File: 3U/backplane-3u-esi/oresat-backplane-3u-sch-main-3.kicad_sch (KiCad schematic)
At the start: 30 parts

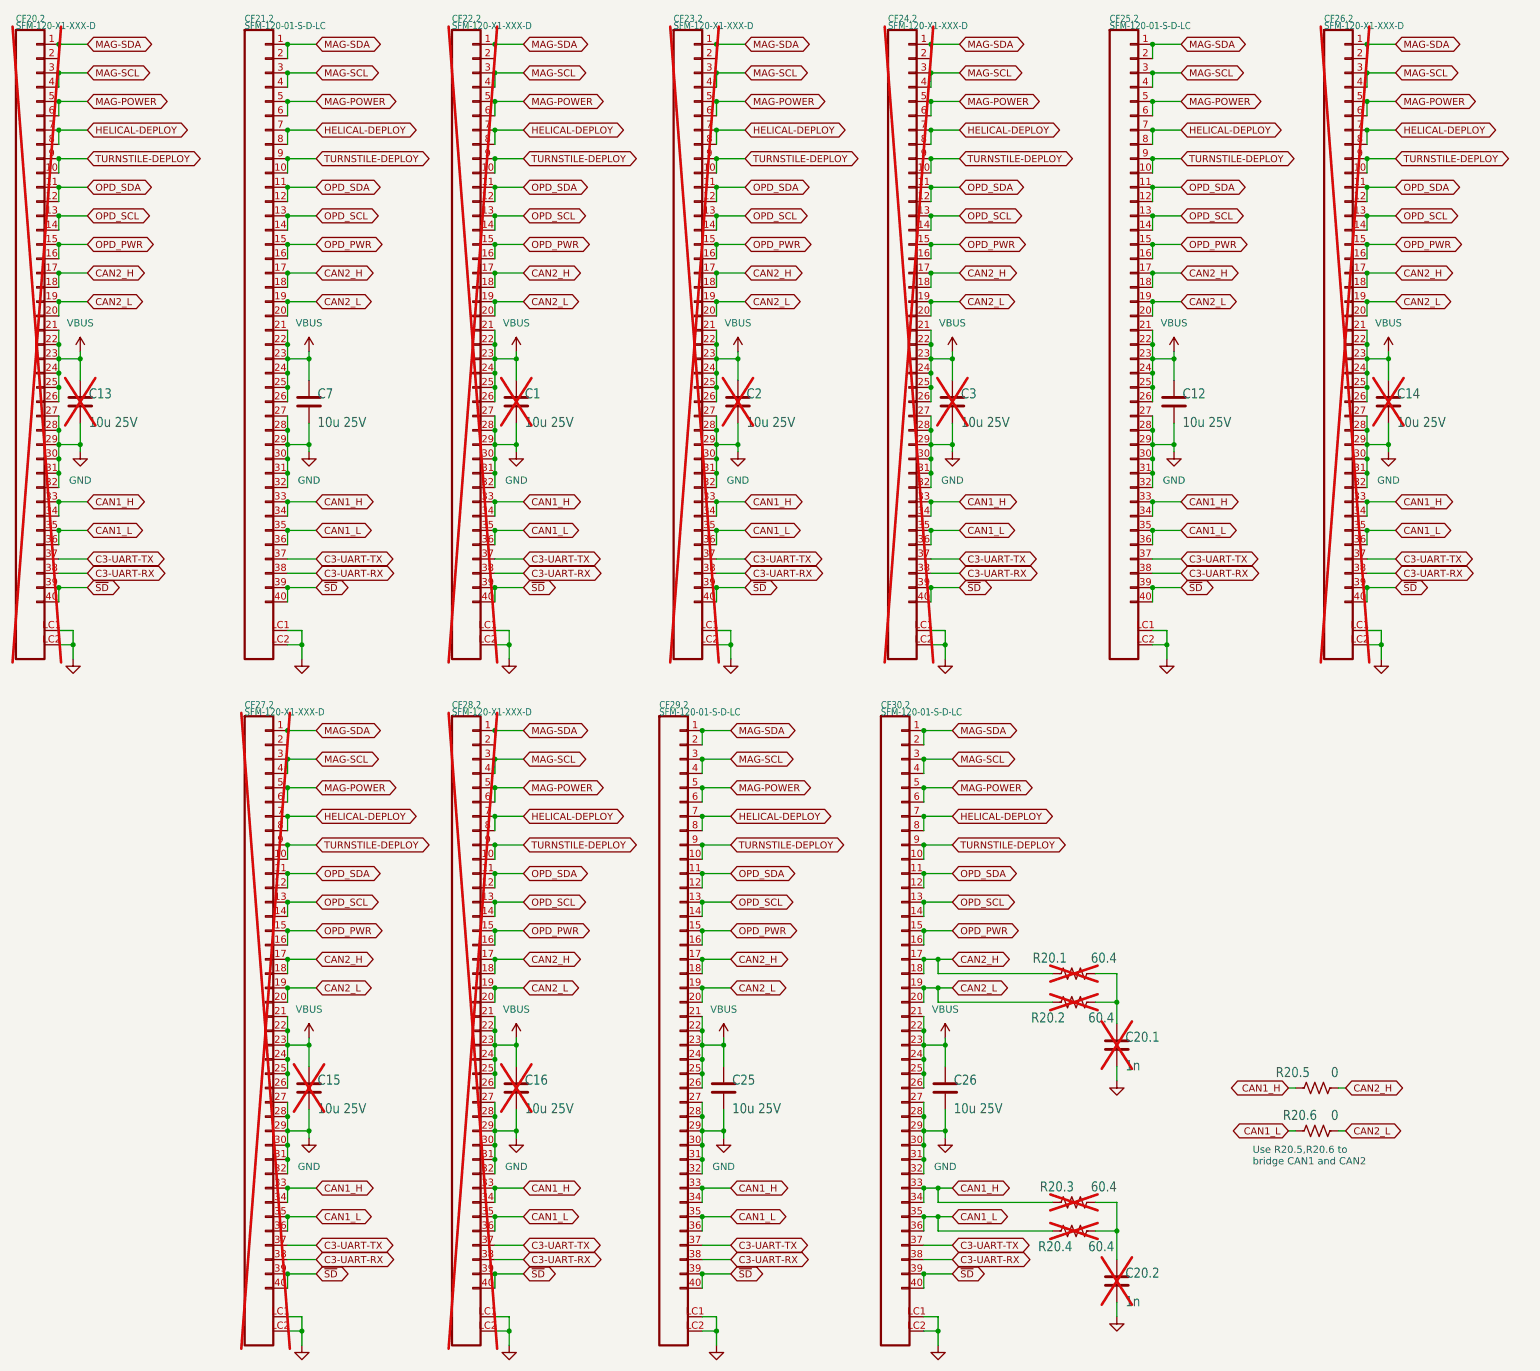
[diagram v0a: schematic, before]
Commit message: Changed schematic & pcb to add spare traces, no helical or turnstile
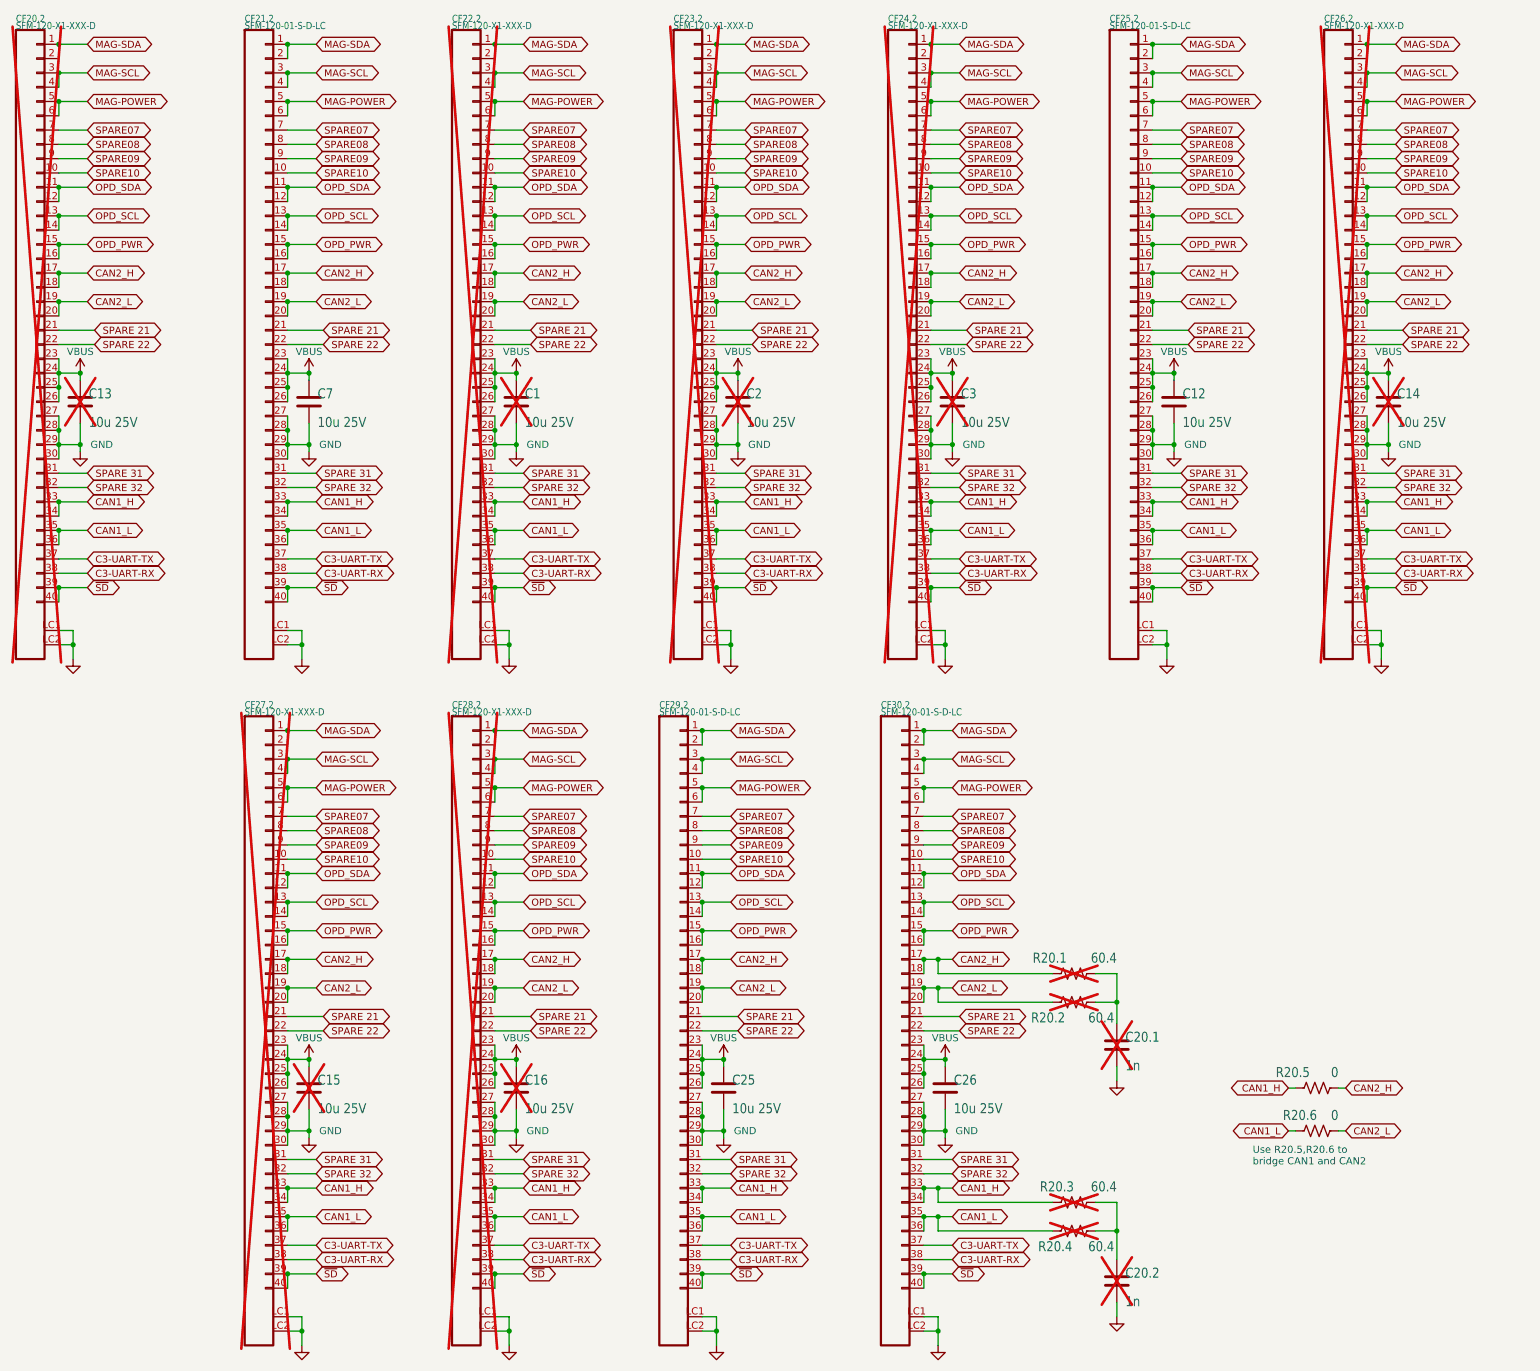
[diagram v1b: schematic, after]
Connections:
- net GND: no longer CF20.2.31, CF20.2.32, CF21.2.31, CF21.2.32, CF22.2.31, CF22.2.32, CF23.2.31, CF23.2.32, CF24.2.31, CF24.2.32, CF25.2.31, CF25.2.32, CF26.2.31, CF26.2.32, CF27.2.31, CF27.2.32, CF28.2.31, CF28.2.32, CF29.2.31, CF29.2.32, CF30.2.31, CF30.2.32
- net VBUS: no longer CF20.2.21, CF20.2.22, CF21.2.21, CF21.2.22, CF22.2.21, CF22.2.22, CF23.2.21, CF23.2.22, CF24.2.21, CF24.2.22, CF25.2.21, CF25.2.22, CF26.2.21, CF26.2.22, CF27.2.21, CF27.2.22, CF28.2.21, CF28.2.22, CF29.2.21, CF29.2.22, CF30.2.21, CF30.2.22
- net HELICAL-DEPLOY renamed SPARE07
- net SPARE07: no longer CF20.2.8, CF21.2.8, CF22.2.8, CF23.2.8, CF24.2.8, CF25.2.8, CF26.2.8, CF27.2.8, CF28.2.8, CF29.2.8, CF30.2.8
- net TURNSTILE-DEPLOY renamed SPARE09
- net SPARE09: no longer CF20.2.10, CF21.2.10, CF22.2.10, CF23.2.10, CF24.2.10, CF25.2.10, CF26.2.10, CF27.2.10, CF28.2.10, CF29.2.10, CF30.2.10
- new net SPARE 21: CF20.2.21, CF21.2.21, CF22.2.21, CF23.2.21, CF24.2.21, CF25.2.21, CF26.2.21, CF27.2.21, CF28.2.21, CF29.2.21, CF30.2.21
- new net SPARE 22: CF20.2.22, CF21.2.22, CF22.2.22, CF23.2.22, CF24.2.22, CF25.2.22, CF26.2.22, CF27.2.22, CF28.2.22, CF29.2.22, CF30.2.22
- new net SPARE 31: CF20.2.31, CF21.2.31, CF22.2.31, CF23.2.31, CF24.2.31, CF25.2.31, CF26.2.31, CF27.2.31, CF28.2.31, CF29.2.31, CF30.2.31
- new net SPARE 32: CF20.2.32, CF21.2.32, CF22.2.32, CF23.2.32, CF24.2.32, CF25.2.32, CF26.2.32, CF27.2.32, CF28.2.32, CF29.2.32, CF30.2.32
- new net SPARE08: CF20.2.8, CF21.2.8, CF22.2.8, CF23.2.8, CF24.2.8, CF25.2.8, CF26.2.8, CF27.2.8, CF28.2.8, CF29.2.8, CF30.2.8
- new net SPARE10: CF20.2.10, CF21.2.10, CF22.2.10, CF23.2.10, CF24.2.10, CF25.2.10, CF26.2.10, CF27.2.10, CF28.2.10, CF29.2.10, CF30.2.10
